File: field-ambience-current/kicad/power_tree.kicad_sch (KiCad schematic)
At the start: 12 parts, among them J1 USB_C_Receptacle (TYPE-C-31-M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, U5 AP7361C-33 1A LDO (+5V->+3V3,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

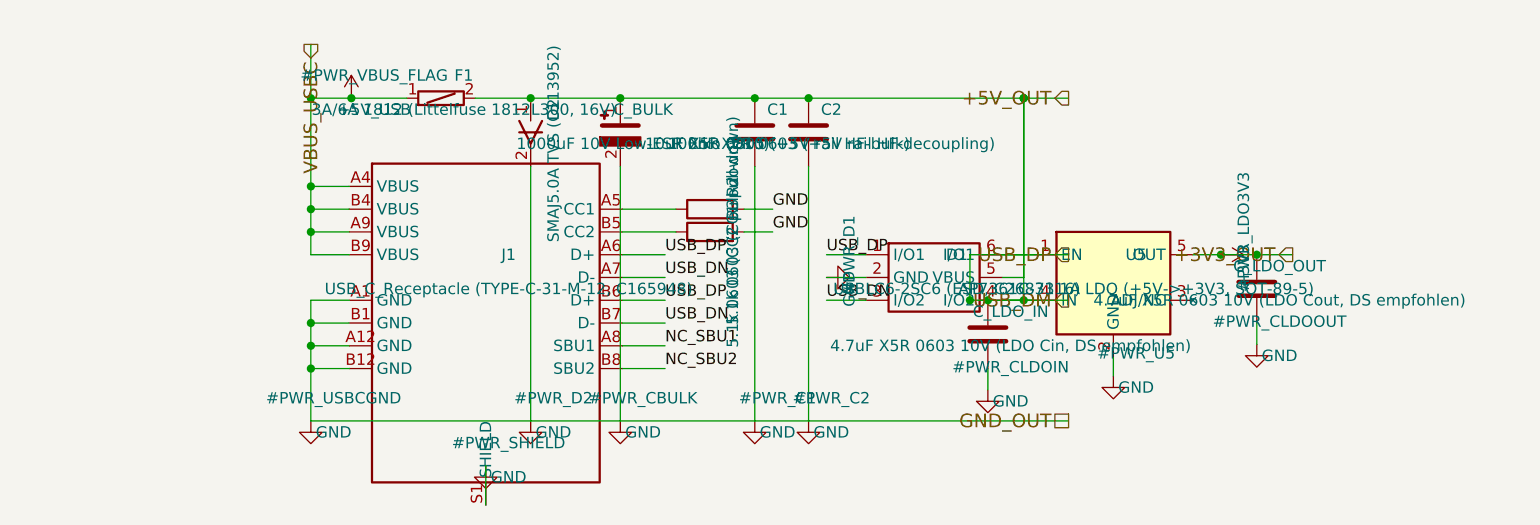
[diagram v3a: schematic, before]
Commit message: pcb(r18.10): Engineering-Realitaetscheck — SW_BOOT, USB-C-Upgrade, BOM-Sync (ADR-0009)
User-Frage: welche Entscheidungen sinnvoll, welche nicht. Vier Fix-Cluster.

=== KRITISCH: BOOT-Button gefehlt ===

Befund: BOOT0 hatte nur 10k-Pulldown. USB-DFU-Flash setzt BOOT0=HIGH
beim Reset voraus -> war physikalisch unmoeglich. SPEC §1-Diagramm
behauptete faelschlich "USB-DFU oder ST-Link".

Fix stm32h743_sheet:
- SW_BOOT (Switch:SW_Push, TS-1185A-C-A / C720477) Pin1 -> BOOT0_PIN
- R_BOOT_SW 1k 0603 (C21190) zwischen SW_BOOT-Pin2 und +3V3
- 1k-Serie limitiert Querstrom auf 3 mA falls SW_RESET gleichzeitig gedrueckt
- Bedienung: SW_BOOT halten -> NRST tippen -> loslassen -> System-Boot-Loader

ST-Link via SWD-Header bleibt Primaer-Programmer; USB-DFU ist Backup
fuer End-User-Service-Updates.

=== USB-C-Stecker upgegradet ===

C165948 (TYPE-C-31-M-12, ~5k Cycles, Generic) ->
C165935 (TYPE-C-31-M-17, 10k Cycles, gleicher HRO-Footprint).

Drop-in laut HRO-Tabelle; in Phase 6 visuell gegen M-17-Drawing pruefen.
Premium-Pfad (GCT USB4135-03-A / Amphenol 12401610E4-2A) fuer Serie
dokumentiert (eigene FPs noetig).

=== SPEC §4 BOM Drift ===

Generator r18.9 hatte Choc-Cells + Stabilizer + SW12-BOOTSEL bereits
entfernt; SPEC-Doku noch alt.

Sync:
- SW1-5 (Choc) -> durchgestrichen + J_CELL1-5 + R_CELL + C_CELL (FSR-IF)
- STAB1-5 -> durchgestrichen
- SW12 BOOTSEL (Pico-spezifisch) -> durchgestrichen
- SW_BOOT + R_BOOT_SW als neue Zeilen
- mechanical_coordinates §4 als veraltet markiert (Maintainer-Hinweis)

=== ADR-0009 NEU ===

Engineering-Review-Doku: alle Befunde + Maßnahmen, Display-SPI1-
Funktionsfaehigkeit verifiziert, Z-Hoehen-Layout-Constraints
(C_BULK 10.5mm <-> LCD-Header 8.5mm Kollision), LED-Farben-Realitaet
(JLC Basic nur weiss, gelb/gruen Extended), FSR-FFC-Empfehlung
(vertagt bis Mechanik-Phase), plus bewusste "aendern wir nicht"-
Entscheidungen.

=== Validierung ===

paren-balance 8/8 PASS - Hier↔Root-Crossref 7/7 PASS - SW_BOOT-Pin1
auf BOOT0_PIN-Rail verdrahtet (Wire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
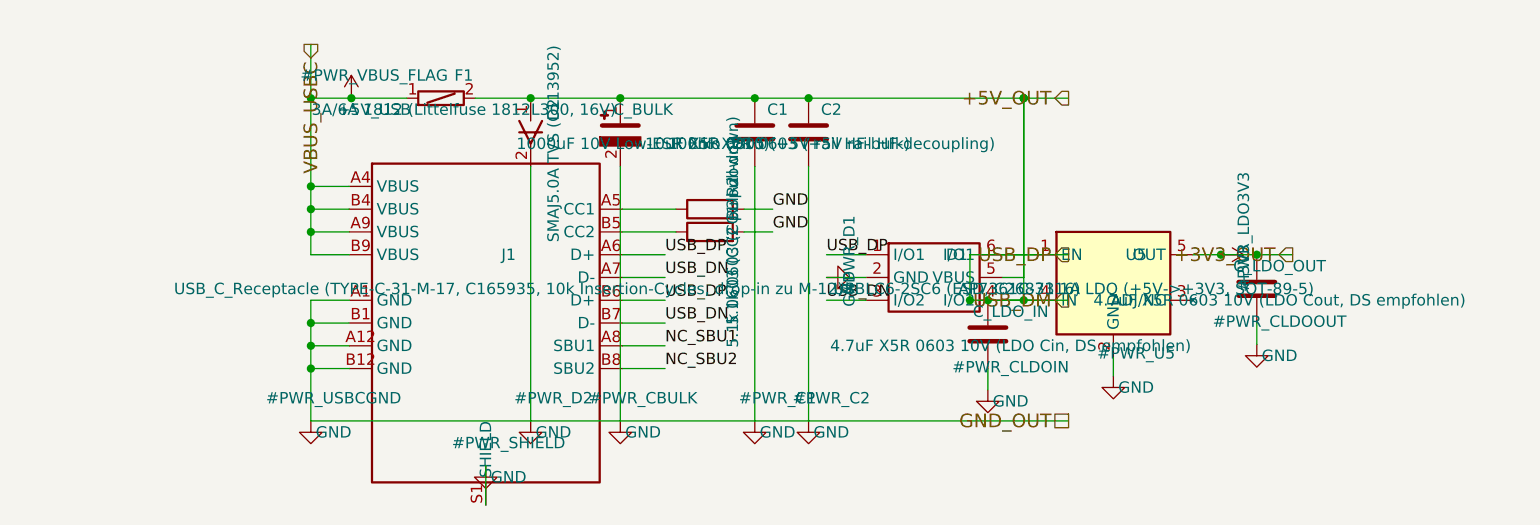
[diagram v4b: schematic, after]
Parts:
- J1: value USB_C_Receptacle (TYPE-C-31-M-12, C165948) -> USB_C_Receptacle (TYPE-C-31-M-17, C165935, 10k Insertion-Cycles, drop-in zu M-12); LCSC C165948 -> C165935; MPN TYPE-C-31-M-12 -> TYPE-C-31-M-17; Notes (none) -> r18.10: Upgrade von C165948 (M-12 / 5k Cycles) auf M-17 (10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
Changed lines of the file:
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@@
       (property "Reference" "J1" (at 52.54 77.46 0)
         (effects (font (size 1.27 1.27))))
-      (property "Value" "USB_C_Receptacle (TYPE-C-31-M-12, C165948)" (at 52.54 81.27 0)
+      (property "Value" "USB_C_Receptacle (TYPE-C-31-M-17, C165935, 10k Insertion-Cycles, drop-in zu M-12)" (at 52.54 81.27 0)
         (effects (font (size 1.27 1.27))))
       (property "Footprint" "Connector_USB:USB_C_Receptacle_HRO_TYPE-C-31-M-12" (at 50.0 80.0 0)
         (effects (font (size 1.27 1.27)) hide))
-      (property "Datasheet" "https://datasheet.lcsc.com/lcsc/2004081102_Korean-Hroparts-Elec-TYPE-C-31-M-12_C165948.pdf" (at 50.0 80.0 0)
+      (property "Datasheet" "https://datasheet.lcsc.com/lcsc/2204262207_Korean-Hroparts-Elec-TYPE-C-31-M-17_C165935.pdf" (at 50.0 80.0 0)
         (effects (font (size 1.27 1.27)) hide))
-      (property "MPN" "TYPE-C-31-M-12" (at 52.54 83.81 0)
+      (property "MPN" "TYPE-C-31-M-17" (at 52.54 83.81 0)
         (effects (font (size 1.27 1.27)) hide))
-      (property "LCSC" "C165948" (at 52.54 85.08 0)
+      (property "LCSC" "C165935" (at 52.54 85.08 0)
+        (effects (font (size 1.27 1.27)) hide))
+      (property "Notes" "r18.10: Upgrade von C165948 (M-12 / 5k Cycles) auf M-17 (10k Cycles). Footprint M-12 ist drop-in kompatibel (laut HRO-Tabelle); pre-fab in Phase 6 visuell gegen M-17-Drawing prüfen." (at 52.54 86.35 0)
         (effects (font (size 1.27 1.27)) hide))
     (instances

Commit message: pcb(r18.12): Pre-Layout-Cleanup — Polymer-Bulk-Cap + EC11J Custom-Draft-FP
Zwei offene Pre-Layout-Punkte adressiert.

=== C_BULK Polymer-Wechsel (loest ADR-0011 Konflikt) ===

1000uF Alu-Elko (10.5mm Hoehe — passte nicht in 8mm-Top-Zone) ersetzt durch:
- C_BULK: 470uF 16V Polymer in EIA-7343-31 (D-Case, ~2mm Hoehe, ESR<15mOhm)
- C_BULK2: 220uF 10V X5R MLCC 1210 parallel

Effektive Bulk-Kapazitaet ~690uF, aber ESR ~10mOhm statt ~25mOhm beim Alu.
Class-D-Bass-Transienten sauberer (ADR-0010 Punkt 4 Anti-Kratzig-Hebel
verstaerkt). Title-Block-Comment synchronisiert.

LCSC-Nummern noch TBD-VERIFY: Panasonic SVPF / Kemet T520D fuer Polymer;
CL32A227KQVNNNE-Klasse fuer 220uF MLCC. Vor BOM-Freeze final pruefen.

=== EC11J Custom-Footprint (FP_VERIFY letzter Punkt) ===

libraries/field_ambience.pretty/RotaryEncoder_ALPS_EC11J_SMD.kicad_mod NEU:
- aus dokumentierten ALPS-EC11J-Standard-Maßen (12x13.4mm Body, 20mm Schaft)
- 5 SMD-Pads + 2 Mounting-Tabs
- Pad-Pitch 2.5mm, Pad 1.4x1.4mm, Mounting-Tabs 1.8x3mm bei +-6mm
- Status FP_DRAFT (nicht FP_NOTE) — vor Fab gegen EasyEDA-Export von
  C209762 verifizieren (Property im Schematic markiert)

4 Encoder-Instanzen referenzieren jetzt den Custom-FP statt des KiCad-
Standard-EC11E-THT-FP (der ohnehin nicht zur SMD-Bauform passte).

=== Validierung ===

paren 8/8 PASS - Crossref 7/7 PASS - 4 Encoder-Instanzen mit neuem FP,
0 EC11E-Reste - Polymer + MLCC parallel sauber im power_tree platziert -
Title-Block-stale-Kommentar gefixt.

=== Scores ===

- Footprint-Verifikation 8 -> 9 (EC11J Draft-FP geschlossen)
- Mechanical / Enclosure 4 -> 5 (C_BULK-Konflikt aufgeloest)
- BOM-Sourcing 7.5 -> 8 (Polymer-Familie identifiziert)

KEIN .kicad_pcb. PR #35 ist jetzt review-ready: 9 Commits von r18.5 bis
r18.12 plus Repo-Phase-1-Refactor, 12 ADRs, alle Schematic-Validierungen
gruen. Empfehlung: PR mergen und r18.13 mit Repo-Refactor Phase 2 (Doc-
Moves) oder Firmware-HAL-Abstraktion starten.

https://claude.ai/code/session_01K5kLTFpDCCoYwx2dq6Rk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
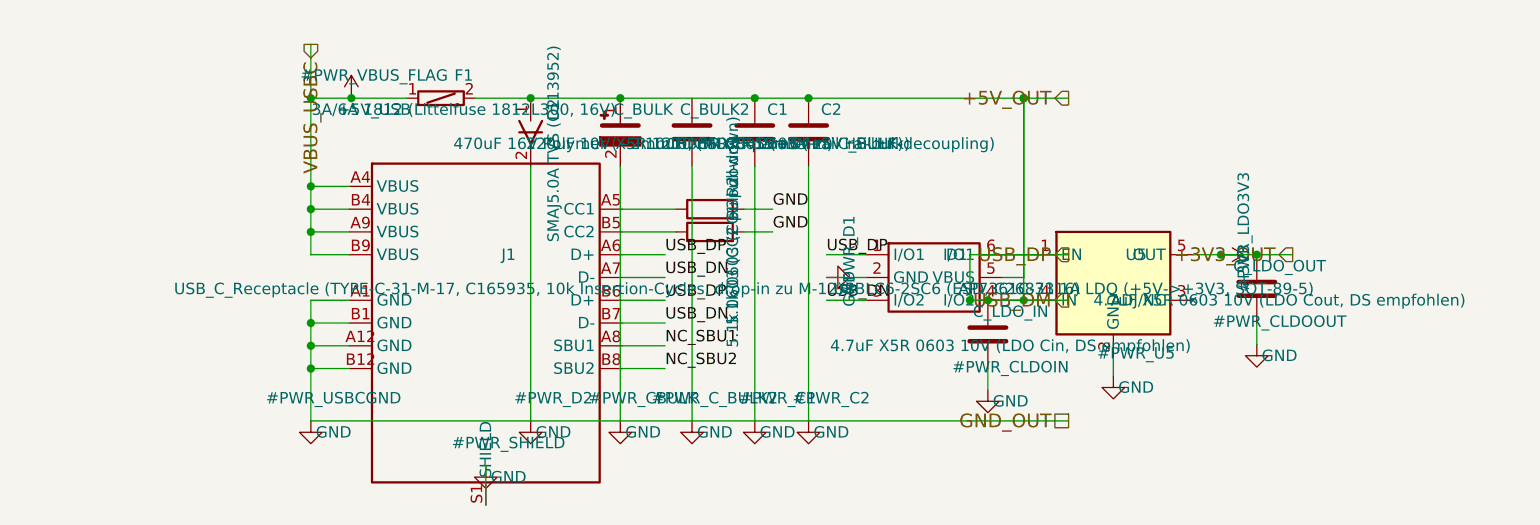
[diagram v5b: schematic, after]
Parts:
- added C_BULK2: 220uF 10V X5R 1210 (MLCC parallel zu C_BULK), Capacitor_SMD:C_1210_3225Metric, symbol Device:C
- C_BULK: value 1000uF 10V Low-ESR Elko (D10) -> 470uF 16V Polymer (~2mm H, ESR<=15mOhm); footprint Capacitor_SMD:CP_Elec_10x10.5 -> Capacitor_SMD:CP_Tantalum_Case-D_EIA-7343-31_Reflow; LCSC C46550395 -> TBD-VERIFY (JLC-Stock vor Layout pruefen); MPN JVJ16V1000M10x10 (1000uF 16V SMD, D10x10.5) -> TBD-VERIFY (Panasonic SVPF-Familie oder Kemet T520D Polymer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; Notes (none) -> r18.12 (ADR-0011): Polymer statt 1000uF Alu — passt in 8mm-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
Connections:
- net GND: now also C_BULK2.2
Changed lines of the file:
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@@
     (company "Field Ambience Project")
     (comment 1 "Per SPEC v0.6.3 §1 + §3")
-    (comment 2 "USB-C → F1(3A/6A) → C_BULK(1000µF) → +5V rail")
+    (comment 2 "USB-C → F1(3A/6A) → C_BULK(470µF Polymer + 220µF MLCC) → +5V rail")
     (comment 3 "USB-C VBUS/GND-Pin-Belegung per USB Type-C Spec Rev 2.1 (v0.6.3 fix)")
     (comment 4 "ESD: USBLC6-2SC6 on D+/D-; TVS: SMAJ5.0A on +5V"))
@@
       (property "Reference" "C_BULK" (at 67.54 61.27 0)
         (effects (font (size 1.27 1.27))))
-      (property "Value" "1000uF 10V Low-ESR Elko (D10)" (at 67.54 65.08 0)
-        (effects (font (size 1.27 1.27))))
-      (property "Footprint" "Capacitor_SMD:CP_Elec_10x10.5" (at 65 63.81 0)
+      (property "Value" "470uF 16V Polymer (~2mm H, ESR<=15mOhm)" (at 67.54 65.08 0)
+        (effects (font (size 1.27 1.27))))
+      (property "Footprint" "Capacitor_SMD:CP_Tantalum_Case-D_EIA-7343-31_Reflow" (at 65 63.81 0)
         (effects (font (size 1.27 1.27)) hide))
       (property "Datasheet" "~" (at 65 63.81 0)
         (effects (font (size 1.27 1.27)) hide))
-      (property "MPN" "JVJ16V1000M10x10 (1000uF 16V SMD, D10x10.5)" (at 67.54 67.62 0)
-        (effects (font (size 1.27 1.27)) hide))
-      (property "LCSC" "C46550395" (at 67.54 68.89 0)
+      (property "MPN" "TBD-VERIFY (Panasonic SVPF-Familie oder Kemet T520D Polymer-Tantal 470uF/16V)" (at 67.54 67.62 0)
+        (effects (font (size 1.27 1.27)) hide))
+      (property "LCSC" "TBD-VERIFY (JLC-Stock vor Layout pruefen)" (at 67.54 68.89 0)
+        (effects (font (size 1.27 1.27)) hide))
+      (property "Notes" "r18.12 (ADR-0011): Polymer statt 1000uF Alu — passt in 8mm-Top-Zone, besserer ESR. Mit C_BULK2 (220uF MLCC) parallel = ~690uF effective." (at 67.54 70.16 0)
         (effects (font (size 1.27 1.27)) hide))
     (instances
@@
       (project "field_ambience"
         (path "/8f124281-8f89-47ab-aa39-bcbf8f1e5e4d" (reference "#PWR_CBULK") (unit 1)))))
+  (symbol (lib_id "Device:C") (at 73 63.81 0) (unit 1)
+    (in_bom yes) (on_board yes) (dnp no)
+      (property "Reference" "C_BULK2" (at 75.54 61.27 0)
+        (effects (font (size 1.27 1.27))))
+      (property "Value" "220uF 10V X5R 1210 (MLCC parallel zu C_BULK)" (at 75.54 65.08 0)
+        (effects (font (size 1.27 1.27))))
+      (property "Footprint" "Capacitor_SMD:C_1210_3225Metric" (at 73 63.81 0)
+        (effects (font (size 1.27 1.27)) hide))
+      (property "Datasheet" "~" (at 73 63.81 0)
+        (effects (font (size 1.27 1.27)) hide))
+      (property "MPN" "TBD-VERIFY (220uF/10V X5R 1210, z.B. CL32A227KQVNNNE)" (at 75.54 67.62 0)
+        (effects (font (size 1.27 1.27)) hide))
+      (property "LCSC" "TBD-VERIFY" (at 75.54 68.89 0)
+        (effects (font (size 1.27 1.27)) hide))
+    (instances
+      (project "field_ambience"
+        (path "/8f124281-8f89-47ab-aa39-bcbf8f1e5e4d" (reference "C_BULK2") (unit 1)))))
+  (symbol (lib_id "Power:GND") (at 73 96.0 0) (unit 1)
+    (in_bom yes) (on_board yes) (dnp no)
+      (property "Reference" "#PWR_C_BULK2" (at 75.54 93.46 0)
+        (effects (font (size 1.27 1.27))))
+      (property "Value" "GND" (at 75.54 97.27 0)
+        (effects (font (size 1.27 1.27))))
+      (property "Footprint" "" (at 73 96.0 0)
+        (effects (font (size 1.27 1.27)) hide))
+      (property "Datasheet" "~" (at 73 96.0 0)
+        (effects (font (size 1.27 1.27)) hide))
+    (instances
+      (project "field_ambience"
+        (path "/8f124281-8f89-47ab-aa39-bcbf8f1e5e4d" (reference "#PWR_C_BULK2") (unit 1)))))
   (symbol (lib_id "Device:C") (at 80 63.81 0) (unit 1)
     (in_bom yes) (on_board yes) (dnp no)
@@
     (stroke (width 0) (type default))
 )
+  (wire (pts (xy 73 67.62) (xy 73 96.0))
+    (stroke (width 0) (type default))
+)

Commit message: pcb+fw(r18.14): Komponenten-Definition — 3D-Lib, 2 kritische BOM-Fixes, Encoder-Strategie (ADR-0012), Cell-Keys Magnetic-Hall (ADR-0013)
User-Direktive: Komponenten vor Layout definieren, 3D-Daten zu allem, Cells
wie HiChord mit langen Caps + Stabilizern, Encoder-Split + smooth + gleich
hoch + flach (Kick75), Encoder-UX-Bug fixen.

🔴 Kritische BOM-Fixes (via 3D-CAD-Abruf entdeckt):
- USB-C: C165935 war ein STF18N65M5-MOSFET (TO-220F-3)! Korrekt: C283540
  (TYPE-C-31-M-17, LCSC-verifiziert). Falsch seit r18.10.
- SW_BOOT: C720477 ist XUNPU TS-1088-AR02016 (nicht TS-1185A-C-A);
  FP von generisch TL3342 auf EasyEDA-verifiziertes SW_TS1088_SMD.

3D-STEP-Library:
- kicad/libraries/field_ambience.3dshapes/ — 9 Z-/Panel-kritische Modelle
- mechanical/3d_models/MANIFEST.md — Inventar, Höhen, Regenerier-Kommando

ADR-0012 Encoder-Strategie:
- EN3 (Display) einziger mit Push+Detents; EN1/2/4 = EC11E183440C smooth
  (ohne Rastung/Anschlag/Switch). Alle 4 = EC11E THT, gleiche Schaftlänge
  = gleich hoch, Ziel 20-22mm statt 24.5mm (EC11J-STEP-Beleg), Kick75-flach.
- EC11J SMD retired (NRND + zu hoch + Half-Step-Mismatch). FP-Verify: 0 offen.

Encoder-UX-Fix („zwei Klicks für 1%"):
- Bench-Encoder rastet jede halbe Quadratur-Periode → ENC_HALF_STEP Default=1
  (display_hw_test.c), Host-Test pinnt Full-Cycle-Modus explizit.
- encoders.c: per-Encoder substeps (Display 4, Smooth 2) + has_sw-Flag.
- 12/12 Test-Suiten PASS.

ADR-0013 Cell-Keys (ersetzt FSR aus ADR-0006):
- Gateron-LP-Magnetic-Switches (HiChord-Feel) + linearer Hall-Sensor pro
  Cell → Velocity = dPos/dt, Aftertouch firmware-offen. ADC-Pins unverändert.
- Lange Caps ≥2u mit LP-Stabilizern (Spacebar-Prinzip: Switch mittig,
  Support links/rechts).
- Schematic: J_CELL 1×2-FSR-Teiler → 1×3-Hall-Site + 1k-Serien-RC.
- Sensor-Kandidaten DRV5056A4/SS49E mit explizitem PINOUT-VERIFY (AP7361-Lektion).

Modifier-Buttons: SPEC stellt explizit klar — alle 5 identisch, momentary,
Latch-Zustand nur über LEDs (ADR-0008).

Scores: F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
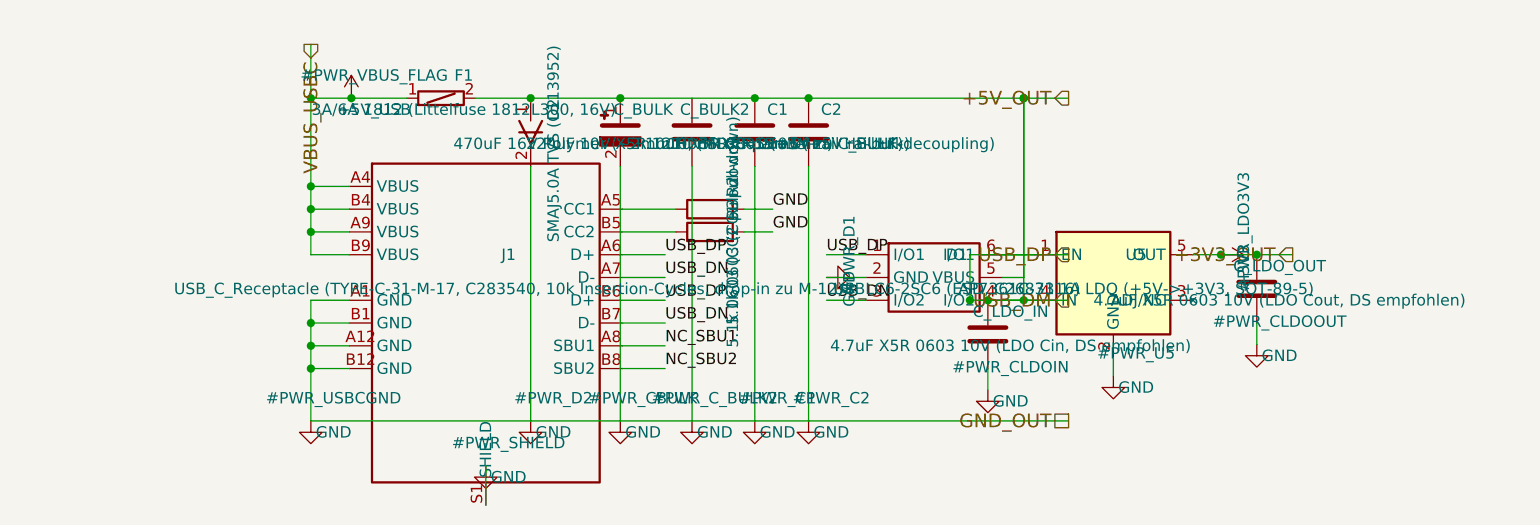
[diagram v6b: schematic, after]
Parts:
- J1: value USB_C_Receptacle (TYPE-C-31-M-17, C165935, 10k Insertion-Cycles, drop-in zu M-12) -> USB_C_Receptacle (TYPE-C-31-M-17, C283540, 10k Insertion-Cycles, drop-in zu M-12); LCSC C165935 -> C283540; Notes r18.10: Upgrade von C165948 (M-12 / 5k Cycles) auf M-17 (10k Cycles). Footprint M-12 ist drop-in kompatibel (laut HRO-Tabelle); pre-fab in Phase 6 visuell gegen M-17-Drawing prüfen. -> r18.10: Upgrade von C165948 (M-12 / 5k Cycles) auf M-17 (10k Cycles). Footprint M-12 ist drop-in kompatibel (laut HRO-Tabelle); pre-fab in Phase 6 visuell gegen M-17-Drawing prüfen. r18.14: LCSC-Nr. korrigiert — C165935 war ein STF18N65M5-MOSFET (TO-220F-3), via EasyEDA-CAD-Verifikation entdeckt. Korrekt: C283540. 3D-STEP in field_ambience.3dshapes (H=3.2mm).
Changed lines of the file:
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@@
       (property "Reference" "J1" (at 52.54 77.46 0)
         (effects (font (size 1.27 1.27))))
-      (property "Value" "USB_C_Receptacle (TYPE-C-31-M-17, C165935, 10k Insertion-Cycles, drop-in zu M-12)" (at 52.54 81.27 0)
+      (property "Value" "USB_C_Receptacle (TYPE-C-31-M-17, C283540, 10k Insertion-Cycles, drop-in zu M-12)" (at 52.54 81.27 0)
         (effects (font (size 1.27 1.27))))
       (property "Footprint" "Connector_USB:USB_C_Receptacle_HRO_TYPE-C-31-M-12" (at 50.0 80.0 0)
         (effects (font (size 1.27 1.27)) hide))
-      (property "Datasheet" "https://datasheet.lcsc.com/lcsc/2204262207_Korean-Hroparts-Elec-TYPE-C-31-M-17_C165935.pdf" (at 50.0 80.0 0)
+      (property "Datasheet" "https://www.lcsc.com/datasheet/lcsc_datasheet_2108131830_Korean-Hroparts-Elec-TYPE-C-31-M-17_C283540.pdf" (at 50.0 80.0 0)
         (effects (font (size 1.27 1.27)) hide))
       (property "MPN" "TYPE-C-31-M-17" (at 52.54 83.81 0)
         (effects (font (size 1.27 1.27)) hide))
-      (property "LCSC" "C165935" (at 52.54 85.08 0)
+      (property "LCSC" "C283540" (at 52.54 85.08 0)
         (effects (font (size 1.27 1.27)) hide))
-      (property "Notes" "r18.10: Upgrade von C165948 (M-12 / 5k Cycles) auf M-17 (10k Cycles). Footprint M-12 ist drop-in kompatibel (laut HRO-Tabelle); pre-fab in Phase 6 visuell gegen M-17-Drawing prüfen." (at 52.54 86.35 0)
+      (property "Notes" "r18.10: Upgrade von C165948 (M-12 / 5k Cycles) auf M-17 (10k Cycles). Footprint M-12 ist drop-in kompatibel (laut HRO-Tabelle); pre-fab in Phase 6 visuell gegen M-17-Drawing prüfen. r18.14: LCSC-Nr. korrigiert — C165935 war ein STF18N65M5-MOSFET (TO-220F-3), via EasyEDA-CAD-Verifikation entdeckt. Korrekt: C283540. 3D-STEP in field_ambience.3dshapes (H=3.2mm)." (at 52.54 86.35 0)
         (effects (font (size 1.27 1.27)) hide))
     (instances
